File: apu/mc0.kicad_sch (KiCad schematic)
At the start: 21 parts, among them U1 X818336-001

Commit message: Internal Connectors
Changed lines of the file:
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@@
 	(bus
 		(pts
-			(xy 252.73 22.86) (xy 257.81 22.86)
+			(xy 252.73 22.86) (xy 255.27 22.86)
 		)
 		(stroke
@@
 	(bus
 		(pts
-			(xy 133.35 22.86) (xy 138.43 22.86)
+			(xy 133.35 22.86) (xy 135.89 22.86)
 		)
 		(stroke
@@
 	(bus
 		(pts
-			(xy 36.83 22.86) (xy 41.91 22.86)
+			(xy 39.37 22.86) (xy 41.91 22.86)
 		)
 		(stroke
@@
 	(bus
 		(pts
-			(xy 156.21 20.32) (xy 161.29 20.32)
+			(xy 158.75 20.32) (xy 161.29 20.32)
 		)
 		(stroke
@@
 	(hierarchical_label "MB{SDRAM}"
 		(shape bidirectional)
-		(at 257.81 22.86 0)
+		(at 255.27 22.86 0)
 		(effects
 			(font
@@
 	(hierarchical_label "MA{SDRAM}"
 		(shape bidirectional)
-		(at 36.83 22.86 180)
+		(at 39.37 22.86 180)
 		(effects
 			(font
@@
 	(hierarchical_label "MA{SDRAM}"
 		(shape bidirectional)
-		(at 138.43 22.86 0)
+		(at 135.89 22.86 0)
 		(effects
 			(font
@@
 	(hierarchical_label "MB{SDRAM}"
 		(shape bidirectional)
-		(at 156.21 20.32 180)
+		(at 158.75 20.32 180)
 		(effects
 			(font

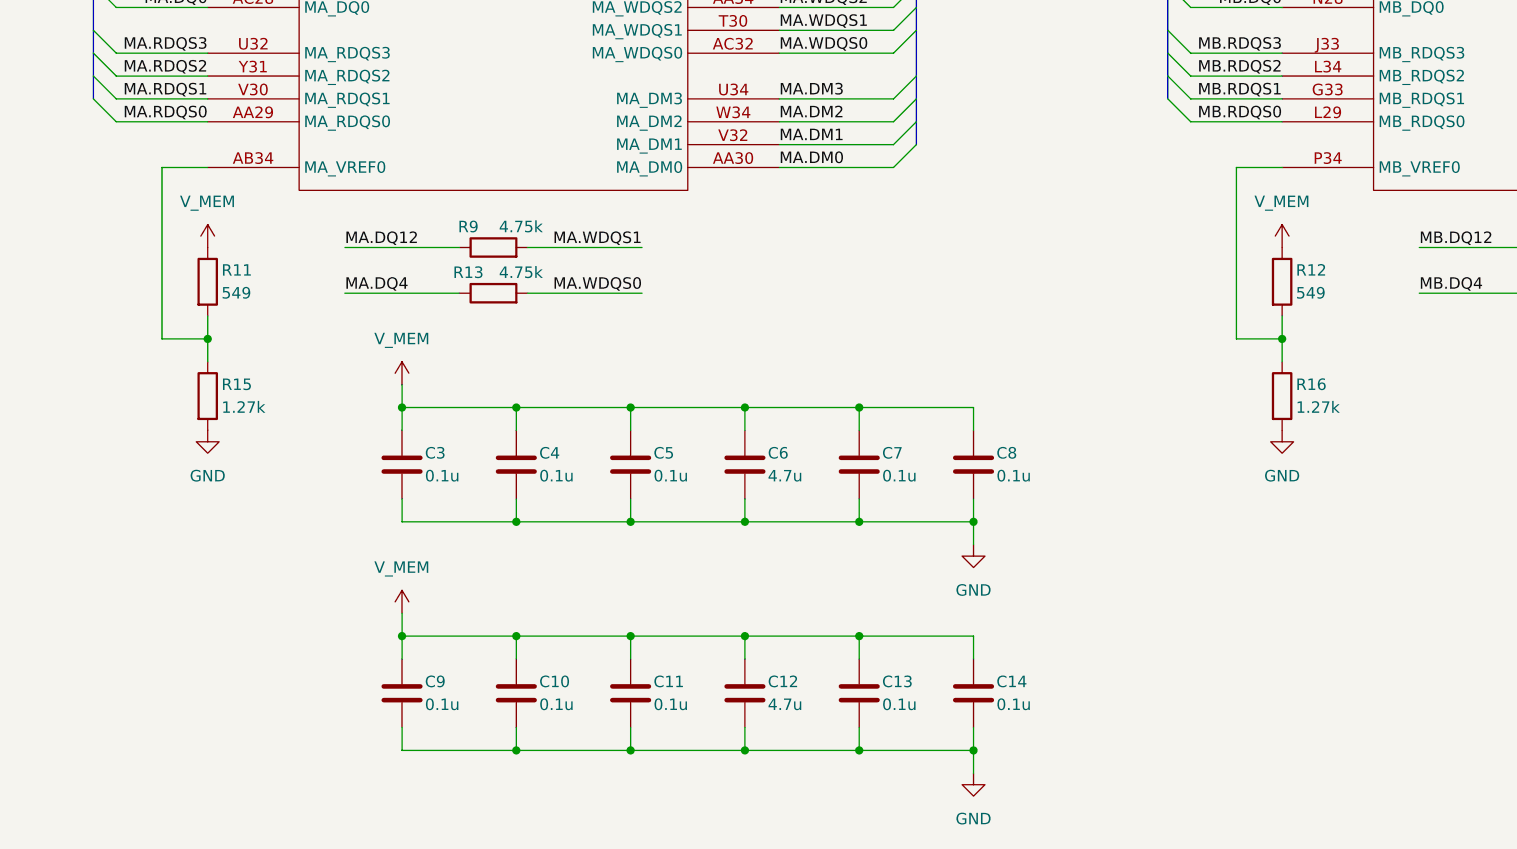
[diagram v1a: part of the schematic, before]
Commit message: Nand Flash, Sata Connectors and removing (hopefully) unnecessary things
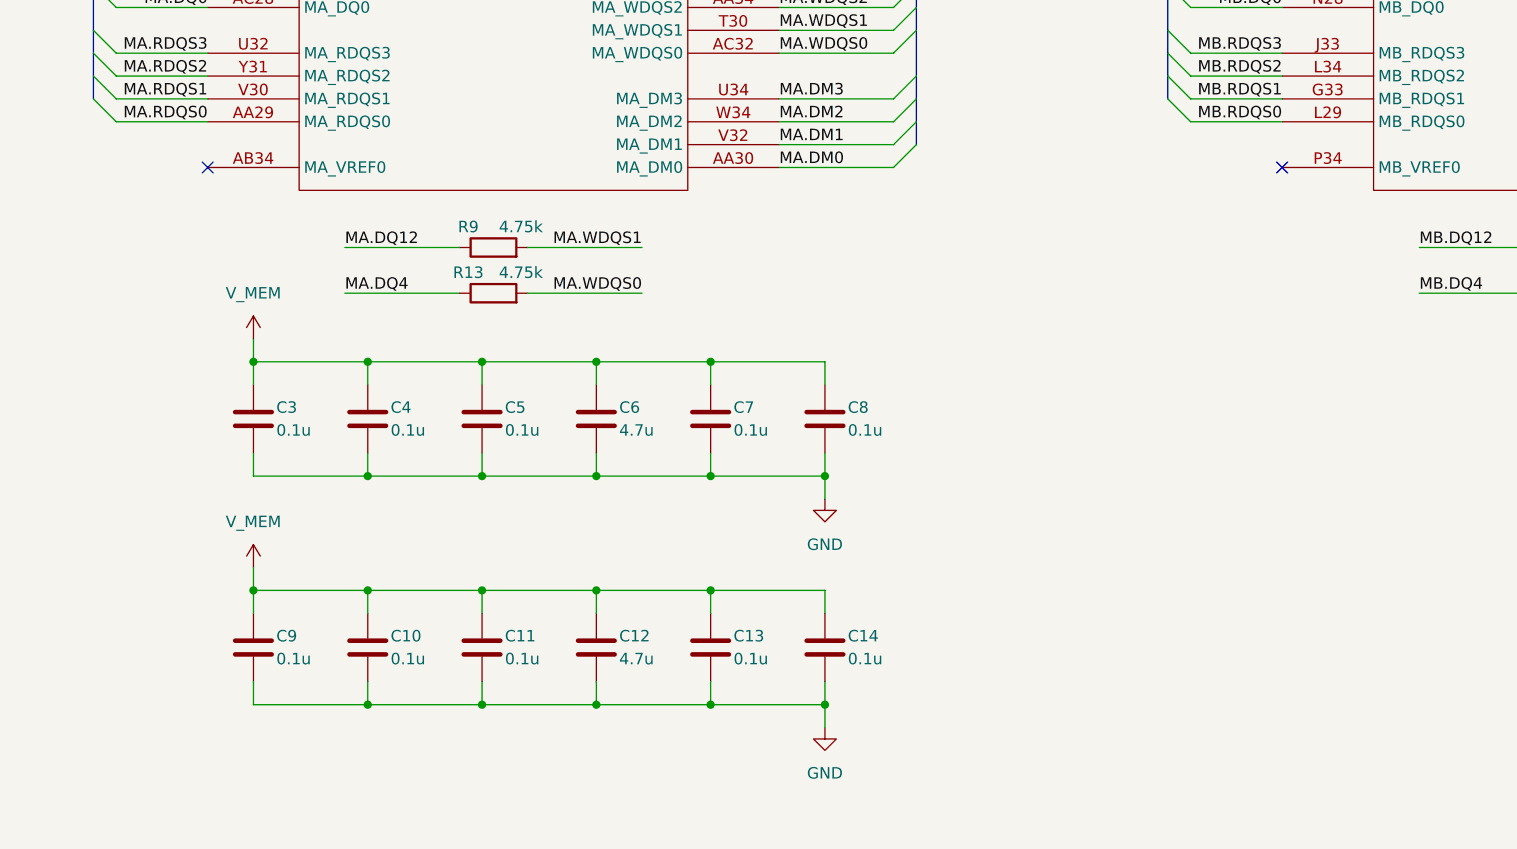
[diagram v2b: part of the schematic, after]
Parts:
- removed R11, R12: 549, symbol Device:R
- removed R15, R16: 1.27k, symbol Device:R
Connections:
- no-connect marks 0 -> 2
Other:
- moved on the sheet: C10, C11, C12, C13, C14, C3, C4, C5, C6, C7, C8, C9

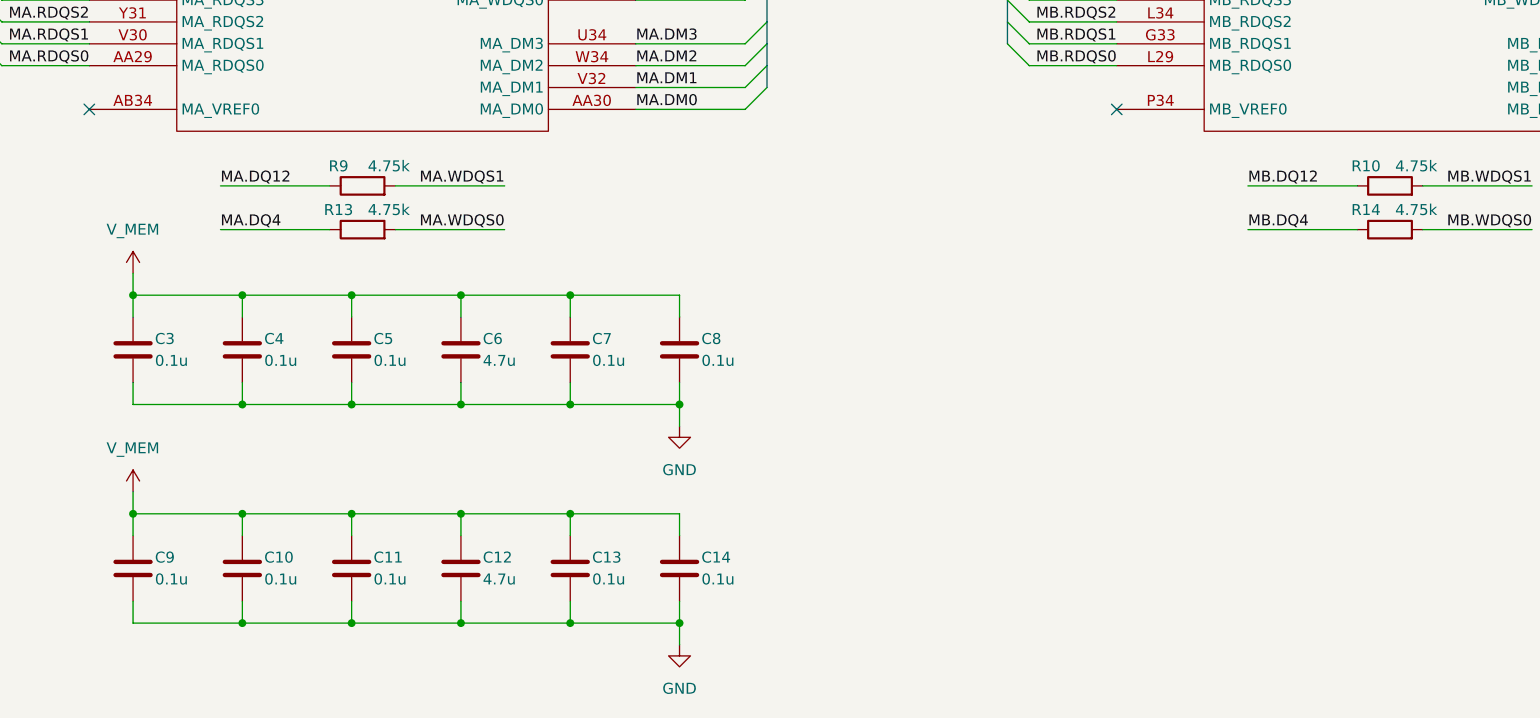
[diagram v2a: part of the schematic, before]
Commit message: Multipurpose and standby power rails, Reannotated schematic
Added V_1P2, V_1P8, V_5P0DUAL, V_EFUSE, V_GPUPCIE, V_3P3STBY and V_1P2STBY
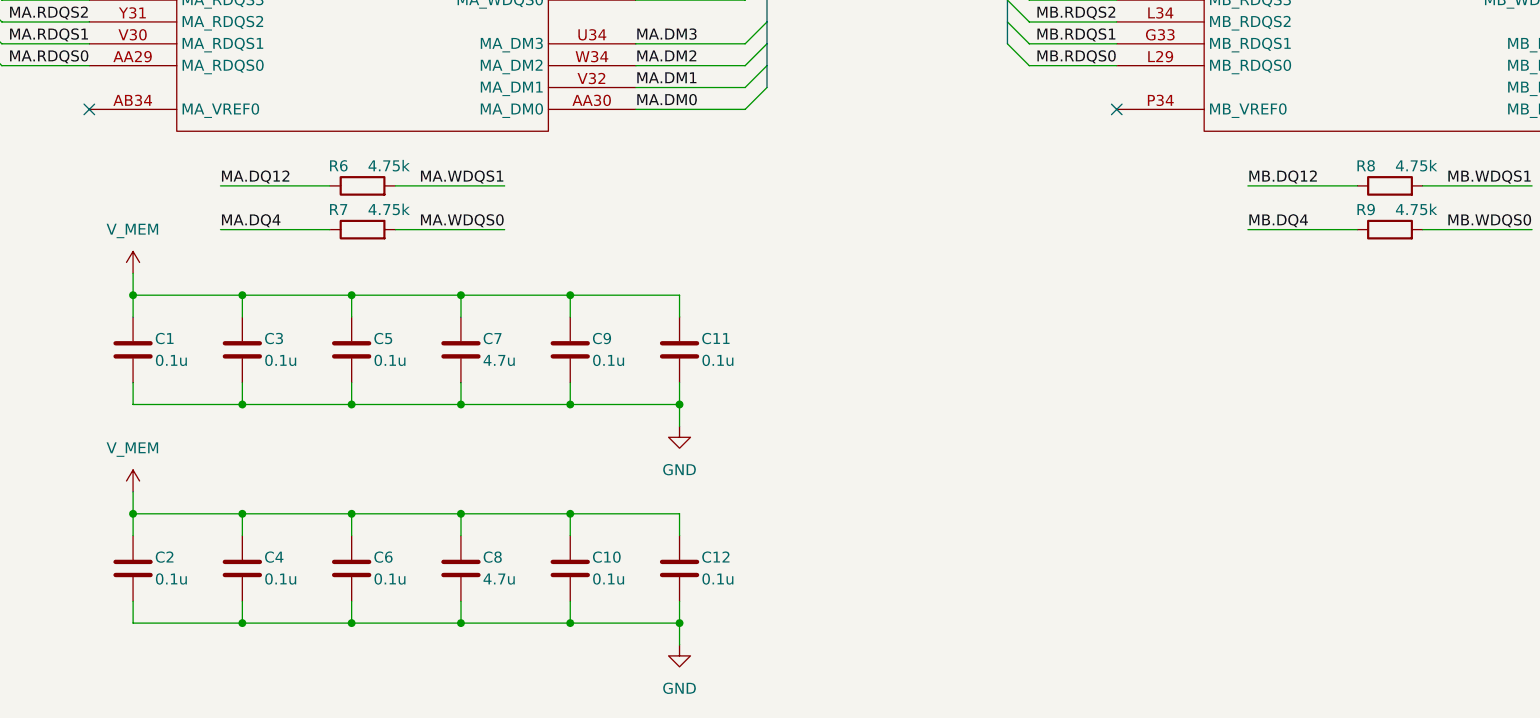
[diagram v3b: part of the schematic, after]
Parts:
- renumbered C3 to C1, C13 to C10, C8 to C11, C14 to C12, C9 to C2, C4 to C3, C10 to C4, C11 to C6, C6 to C7, C12 to C8, C7 to C9, R9 to R6, R13 to R7, R10 to R8, R14 to R9
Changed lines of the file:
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@@
 		(on_board yes)
 		(dnp no)
-		(property "Reference" "C13"
+		(property "Reference" "C10"
 			(at 113.03 173.99 0)
 			(effects
@@
 			(project "StingBurst"
 				(path "/16640ecb-e4a4-4594-871b-70047bfba6e0/15d9acf0-ed9b-44aa-a266-2c44722c6abb/bdd4374f-24d8-4ec0-91f8-4c96c55e95c1"
-					(reference "C13")
+					(reference "C10")
 					(unit 1)
 				)
@@
 		(on_board yes)
 		(dnp no)
-		(property "Reference" "C10"
+		(property "Reference" "C4"
 			(at 74.93 173.99 0)
 			(effects
@@
 			(project "StingBurst"
 				(path "/16640ecb-e4a4-4594-871b-70047bfba6e0/15d9acf0-ed9b-44aa-a266-2c44722c6abb/bdd4374f-24d8-4ec0-91f8-4c96c55e95c1"
-					(reference "C10")
+					(reference "C4")
 					(unit 1)
 				)
@@
 		(on_board yes)
 		(dnp no)
-		(property "Reference" "#PWR012"
+		(property "Reference" "#PWR07"
 			(at 59.69 144.78 0)
 			(effects
@@
 			(project "StingBurst"
 				(path "/16640ecb-e4a4-4594-871b-70047bfba6e0/15d9acf0-ed9b-44aa-a266-2c44722c6abb/bdd4374f-24d8-4ec0-91f8-4c96c55e95c1"
-					(reference "#PWR012")
+					(reference "#PWR07")
 					(unit 1)
 				)
@@
 		(on_board yes)
 		(dnp no)
-		(property "Reference" "C14"
+		(property "Reference" "C12"
 			(at 125.73 173.99 0)
 			(effects
@@
 			(project "StingBurst"
 				(path "/16640ecb-e4a4-4594-871b-70047bfba6e0/15d9acf0-ed9b-44aa-a266-2c44722c6abb/bdd4374f-24d8-4ec0-91f8-4c96c55e95c1"
-					(reference "C14")
+					(reference "C12")
 					(unit 1)
 				)
@@
 		(on_board yes)
 		(dnp no)
-		(property "Reference" "C9"
+		(property "Reference" "C2"
 			(at 62.23 173.99 0)
 			(effects
@@
 			(project "StingBurst"
 				(path "/16640ecb-e4a4-4594-871b-70047bfba6e0/15d9acf0-ed9b-44aa-a266-2c44722c6abb/bdd4374f-24d8-4ec0-91f8-4c96c55e95c1"
-					(reference "C9")
+					(reference "C2")
 					(unit 1)
 				)
@@
 		(on_board yes)
 		(dnp no)
-		(property "Reference" "C6"
+		(property "Reference" "C7"
 			(at 100.33 148.59 0)
 			(effects
@@
 			(project "StingBurst"
 				(path "/16640ecb-e4a4-4594-871b-70047bfba6e0/15d9acf0-ed9b-44aa-a266-2c44722c6abb/bdd4374f-24d8-4ec0-91f8-4c96c55e95c1"
-					(reference "C6")
+					(reference "C7")
 					(unit 1)
 				)
@@
 		(on_board yes)
 		(dnp no)
-		(property "Reference" "C7"
+		(property "Reference" "C9"
 			(at 113.03 148.59 0)
 			(effects
@@
 			(project "StingBurst"
 				(path "/16640ecb-e4a4-4594-871b-70047bfba6e0/15d9acf0-ed9b-44aa-a266-2c44722c6abb/bdd4374f-24d8-4ec0-91f8-4c96c55e95c1"
-					(reference "C7")
+					(reference "C9")
 					(unit 1)
 				)
@@
 		(on_board yes)
 		(dnp no)
-		(property "Reference" "C3"
+		(property "Reference" "C1"
 			(at 62.23 148.59 0)
 			(effects
@@
 			(project "StingBurst"
 				(path "/16640ecb-e4a4-4594-871b-70047bfba6e0/15d9acf0-ed9b-44aa-a266-2c44722c6abb/bdd4374f-24d8-4ec0-91f8-4c96c55e95c1"
-					(reference "C3")
+					(reference "C1")
 					(unit 1)
 				)
@@
 		(dnp no)
 		(fields_autoplaced yes)
-		(property "Reference" "#PWR017"
+		(property "Reference" "#PWR010"
 			(at 123.19 190.5 0)
 			(effects
@@
 			(project "StingBurst"
 				(path "/16640ecb-e4a4-4594-871b-70047bfba6e0/15d9acf0-ed9b-44aa-a266-2c44722c6abb/bdd4374f-24d8-4ec0-91f8-4c96c55e95c1"
-					(reference "#PWR017")
+					(reference "#PWR010")
 					(unit 1)
 				)
@@
 		(on_board yes)
 		(dnp no)
-		(property "Reference" "C8"
+		(property "Reference" "C11"
 			(at 125.73 148.59 0)
 			(effects
@@
 			(project "StingBurst"
 				(path "/16640ecb-e4a4-4594-871b-70047bfba6e0/15d9acf0-ed9b-44aa-a266-2c44722c6abb/bdd4374f-24d8-4ec0-91f8-4c96c55e95c1"
-					(reference "C8")
+					(reference "C11")
 					(unit 1)
 				)
@@
 		(on_board yes)
 		(dnp no)
-		(property "Reference" "C11"
+		(property "Reference" "C6"
 			(at 87.63 173.99 0)
 			(effects
@@
 			(project "StingBurst"
 				(path "/16640ecb-e4a4-4594-871b-70047bfba6e0/15d9acf0-ed9b-44aa-a266-2c44722c6abb/bdd4374f-24d8-4ec0-91f8-4c96c55e95c1"
-					(reference "C11")
+					(reference "C6")
 					(unit 1)
 				)
@@
 		(dnp no)
 		(fields_autoplaced yes)
-		(property "Reference" "#PWR015"
+		(property "Reference" "#PWR09"
 			(at 123.19 165.1 0)
 			(effects
@@
 			(project "StingBurst"
 				(path "/16640ecb-e4a4-4594-871b-70047bfba6e0/15d9acf0-ed9b-44aa-a266-2c44722c6abb/bdd4374f-24d8-4ec0-91f8-4c96c55e95c1"
-					(reference "#PWR015")
+					(reference "#PWR09")
 					(unit 1)
 				)
@@
 		(on_board yes)
 		(dnp no)
-		(property "Reference" "#PWR016"
+		(property "Reference" "#PWR08"
 			(at 59.69 170.18 0)
 			(effects
@@
 			(project "StingBurst"
 				(path "/16640ecb-e4a4-4594-871b-70047bfba6e0/15d9acf0-ed9b-44aa-a266-2c44722c6abb/bdd4374f-24d8-4ec0-91f8-4c96c55e95c1"
-					(reference "#PWR016")
+					(reference "#PWR08")
 					(unit 1)
 				)
@@
 		(on_board yes)
 		(dnp no)
-		(property "Reference" "R9"
+		(property "Reference" "R6"
 			(at 83.566 128.524 90)
 			(effects
@@
 			(project "StingBurst"
 				(path "/16640ecb-e4a4-4594-871b-70047bfba6e0/15d9acf0-ed9b-44aa-a266-2c44722c6abb/bdd4374f-24d8-4ec0-91f8-4c96c55e95c1"
-					(reference "R9")
+					(reference "R6")
 					(unit 1)
 				)
@@
 		(on_board yes)
 		(dnp no)
-		(property "Reference" "R14"
+		(property "Reference" "R9"
 			(at 202.946 133.604 90)
 			(effects
@@
 			(project "StingBurst"
 				(path "/16640ecb-e4a4-4594-871b-70047bfba6e0/15d9acf0-ed9b-44aa-a266-2c44722c6abb/bdd4374f-24d8-4ec0-91f8-4c96c55e95c1"
-					(reference "R14")
+					(reference "R9")
 					(unit 1)
 				)
@@
 		(on_board yes)
 		(dnp no)
-		(property "Reference" "C12"
+		(property "Reference" "C8"
 			(at 100.33 173.99 0)
 			(effects
@@
 			(project "StingBurst"
 				(path "/16640ecb-e4a4-4594-871b-70047bfba6e0/15d9acf0-ed9b-44aa-a266-2c44722c6abb/bdd4374f-24d8-4ec0-91f8-4c96c55e95c1"
-					(reference "C12")
+					(reference "C8")
 					(unit 1)
 				)
@@
 		(on_board yes)
 		(dnp no)
-		(property "Reference" "R13"
+		(property "Reference" "R7"
 			(at 83.566 133.604 90)
 			(effects
@@
 			(project "StingBurst"
 				(path "/16640ecb-e4a4-4594-871b-70047bfba6e0/15d9acf0-ed9b-44aa-a266-2c44722c6abb/bdd4374f-24d8-4ec0-91f8-4c96c55e95c1"
-					(reference "R13")
+					(reference "R7")
 					(unit 1)
 				)
@@
 		(on_board yes)
 		(dnp no)
-		(property "Reference" "C4"
+		(property "Reference" "C3"
 			(at 74.93 148.59 0)
 			(effects
@@
 			(project "StingBurst"
 				(path "/16640ecb-e4a4-4594-871b-70047bfba6e0/15d9acf0-ed9b-44aa-a266-2c44722c6abb/bdd4374f-24d8-4ec0-91f8-4c96c55e95c1"
-					(reference "C4")
+					(reference "C3")
 					(unit 1)
 				)
@@
 		(on_board yes)
 		(dnp no)
-		(property "Reference" "R10"
+		(property "Reference" "R8"
 			(at 202.946 128.524 90)
 			(effects
@@
 			(project "StingBurst"
 				(path "/16640ecb-e4a4-4594-871b-70047bfba6e0/15d9acf0-ed9b-44aa-a266-2c44722c6abb/bdd4374f-24d8-4ec0-91f8-4c96c55e95c1"
-					(reference "R10")
+					(reference "R8")
 					(unit 1)
 				)
